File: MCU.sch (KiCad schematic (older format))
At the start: 64 parts, among them J9 Micro_SD_Card_Det_Hirose_DM3AT, SW1 RESET, U11 STM32G474, U12 M95256-WMN6P, U17 ADG706, U5 MCP2562, U6 LTC6259, U8 LTC6820, U9 HM2103

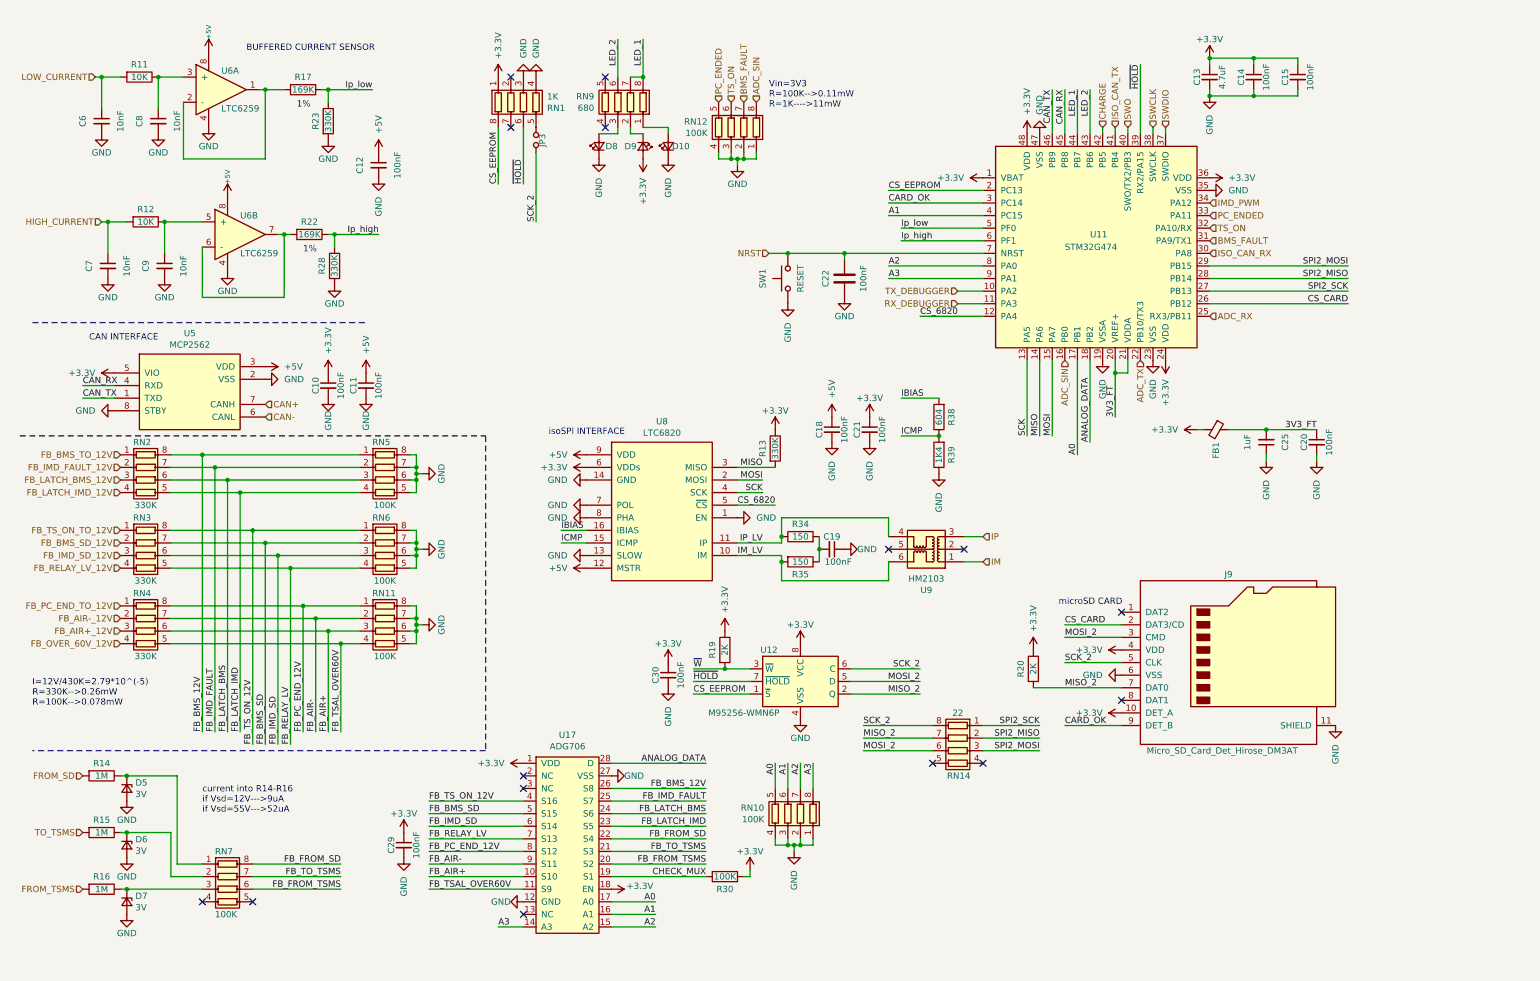
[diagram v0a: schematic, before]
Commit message: added a lot of annotations and readability in the schematic, not complete
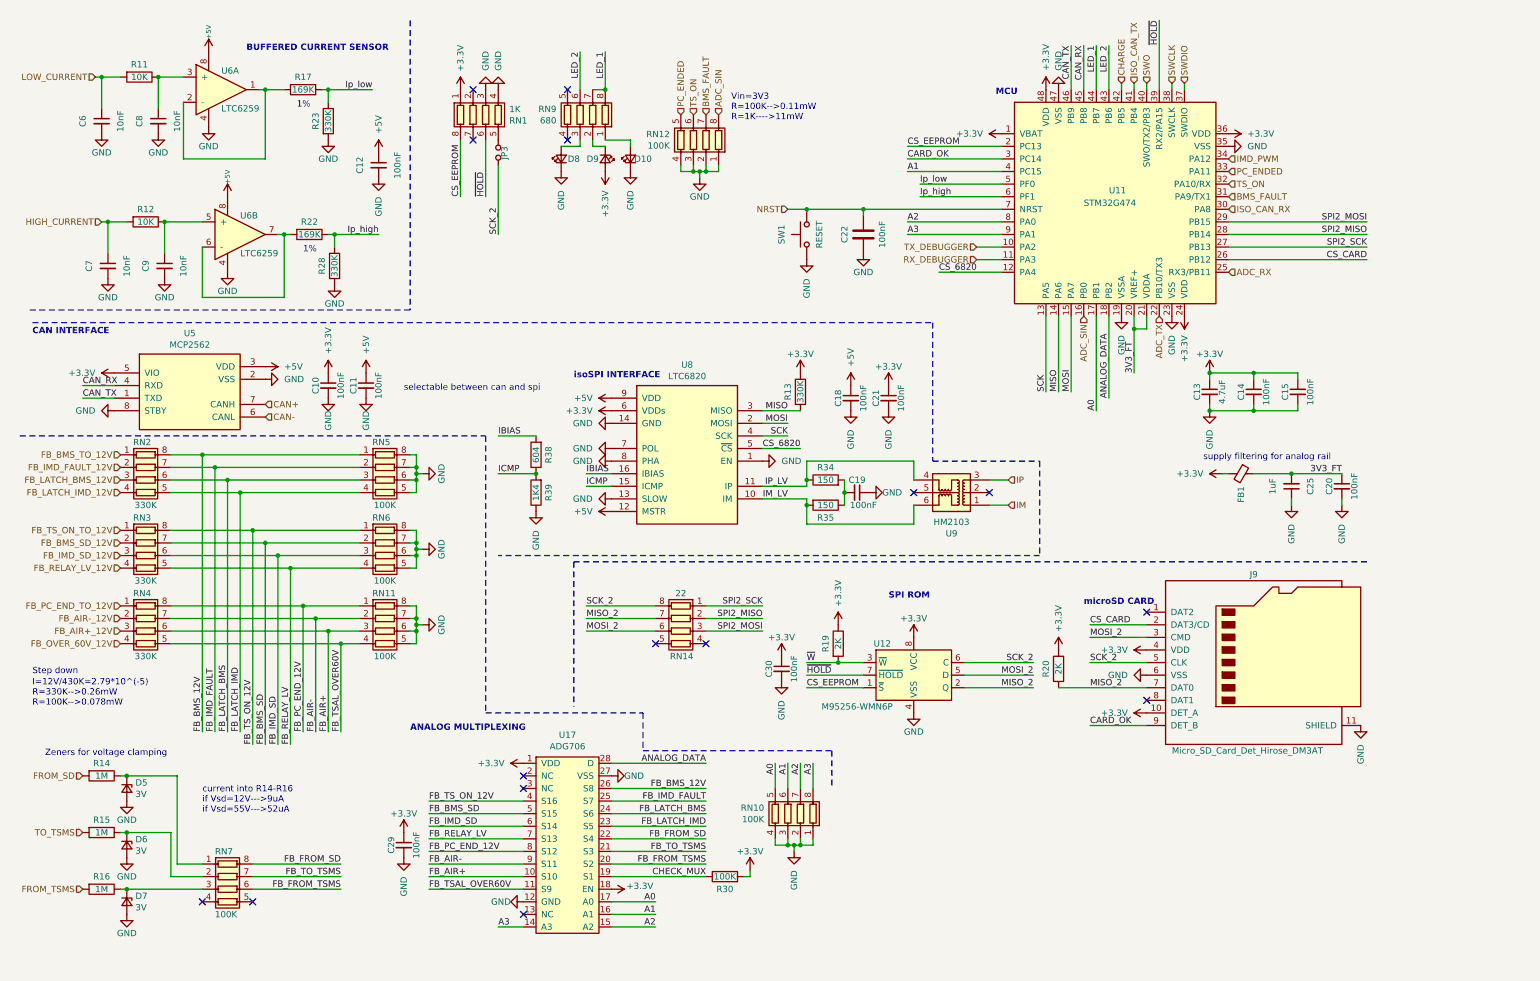
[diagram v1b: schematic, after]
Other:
- note added: "ANALOG MULTIPLEXING"
- note added: "MCU"
- note added: "SPI ROM"
- note added: "Step down"
- note added: "Zeners for voltage clamping"
- note added: "selectable between can and spi"
- note added: "supply filtering for analog rail"
- moved on the sheet: C13, C14, C15, C18, C19, C20, C21, C22, C25, C30, D10, D8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

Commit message: Updated the project to updates in the kicad libraries
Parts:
- FB1: value Ferrite_Bead_Small -> FerriteBead_Small; symbol Device:Ferrite_Bead_Small -> Device:FerriteBead_Small
- JP3: value Jumper_NO_Small -> SolderJumper_2_Open; symbol Device:Jumper_NO_Small -> Jumper:SolderJumper_2_Open
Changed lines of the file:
@@
 $EndComp
 $Comp
-L Device:Ferrite_Bead_Small FB1
+L Device:FerriteBead_Small FB1
 U 1 1 5E60756E
 P 10200 4100
 F 0 "FB1" H 10300 4100 50  0000 L CNN
-F 1 "Ferrite_Bead_Small" H 10300 4055 50  0001 L CNN
+F 1 "FerriteBead_Small" H 10300 4055 50  0001 L CNN
 F 2 "Inductor_SMD:L_0603_1608Metric_Pad1.05x0.95mm_HandSolder" V 10130 4100 50  0001 C CNN
 F 3 "~" H 10200 4100 50  0001 C CNN
@@
 $EndComp
 Wire Wire Line
-	4300 1650 4300 2200
-$Comp
-L Device:Jumper_NO_Small JP3
+	4300 1750 4300 2200
+$Comp
+L Jumper:SolderJumper_2_Open JP3
 U 1 1 5EB0119F
-P 4300 1550
-F 0 "JP3" H 4250 1500 50  0000 L CNN
-F 1 "Jumper_NO_Small" V 4345 1598 50  0001 L CNN
-F 2 "MainBoard:Jumper_SMD_0603" H 4300 1550 50  0001 C CNN
-F 3 "~" H 4300 1550 50  0001 C CNN
-	1    4300 1550
+P 4300 1600
+F 0 "JP3" H 4250 1550 50  0000 L CNN
+F 1 "SolderJumper_2_Open" V 4345 1648 50  0001 L CNN
+F 2 "MainBoard:Jumper_SMD_0603" H 4300 1600 50  0001 C CNN
+F 3 "~" H 4300 1600 50  0001 C CNN
+	1    4300 1600
 	0    -1   1    0
 $EndComp

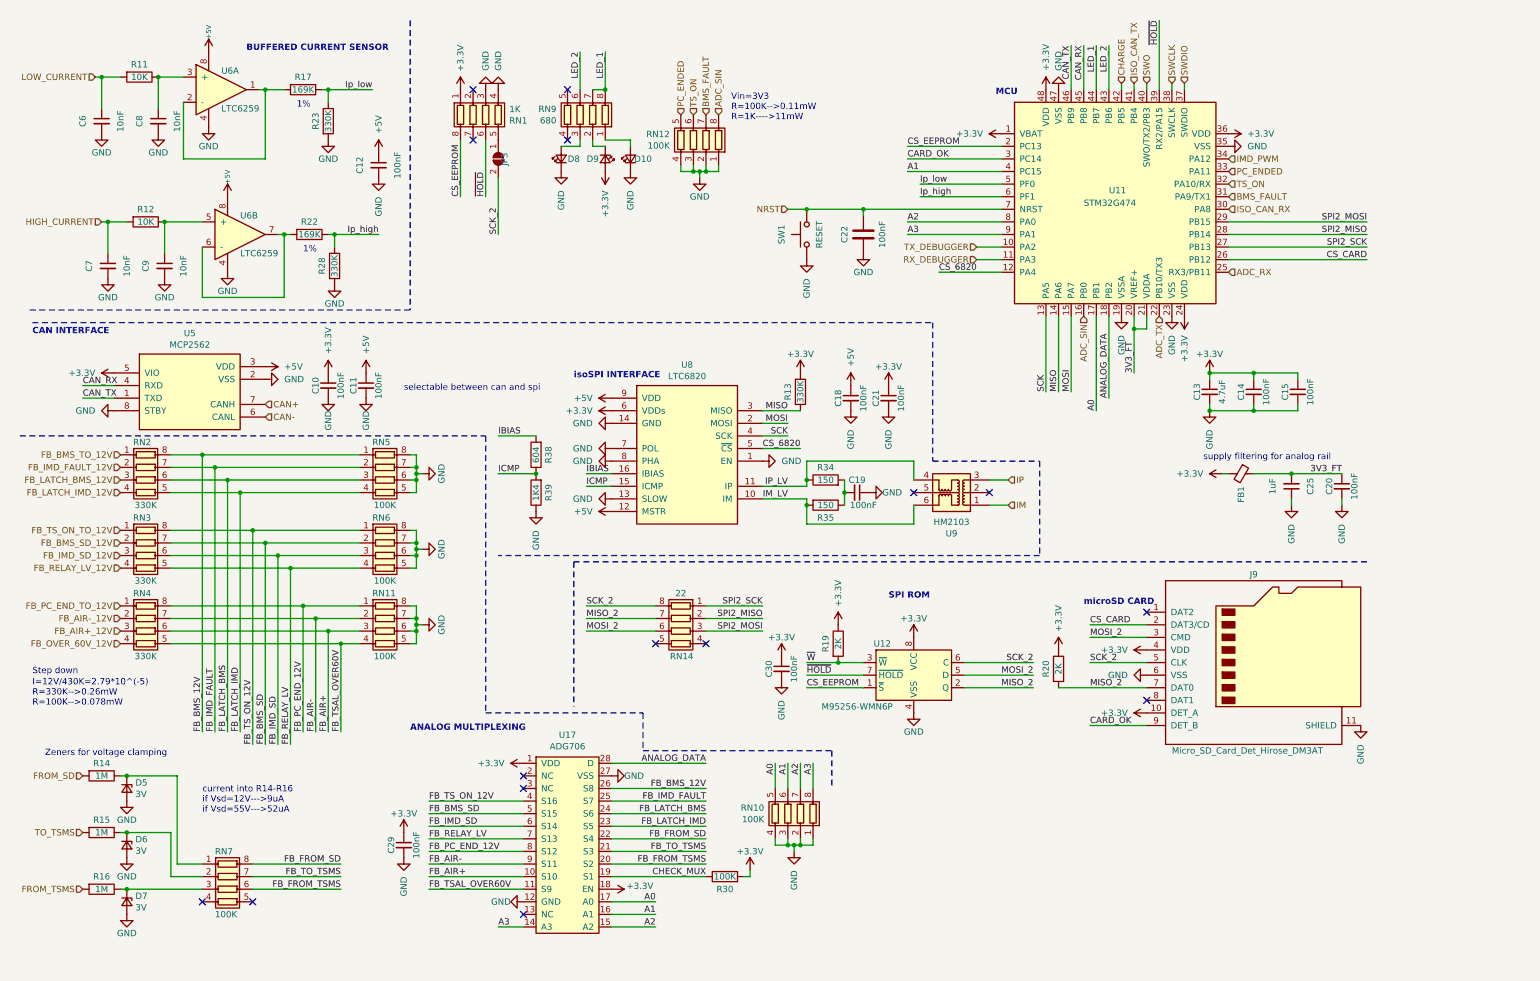
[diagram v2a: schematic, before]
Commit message: updated to new components as per v1.0.5
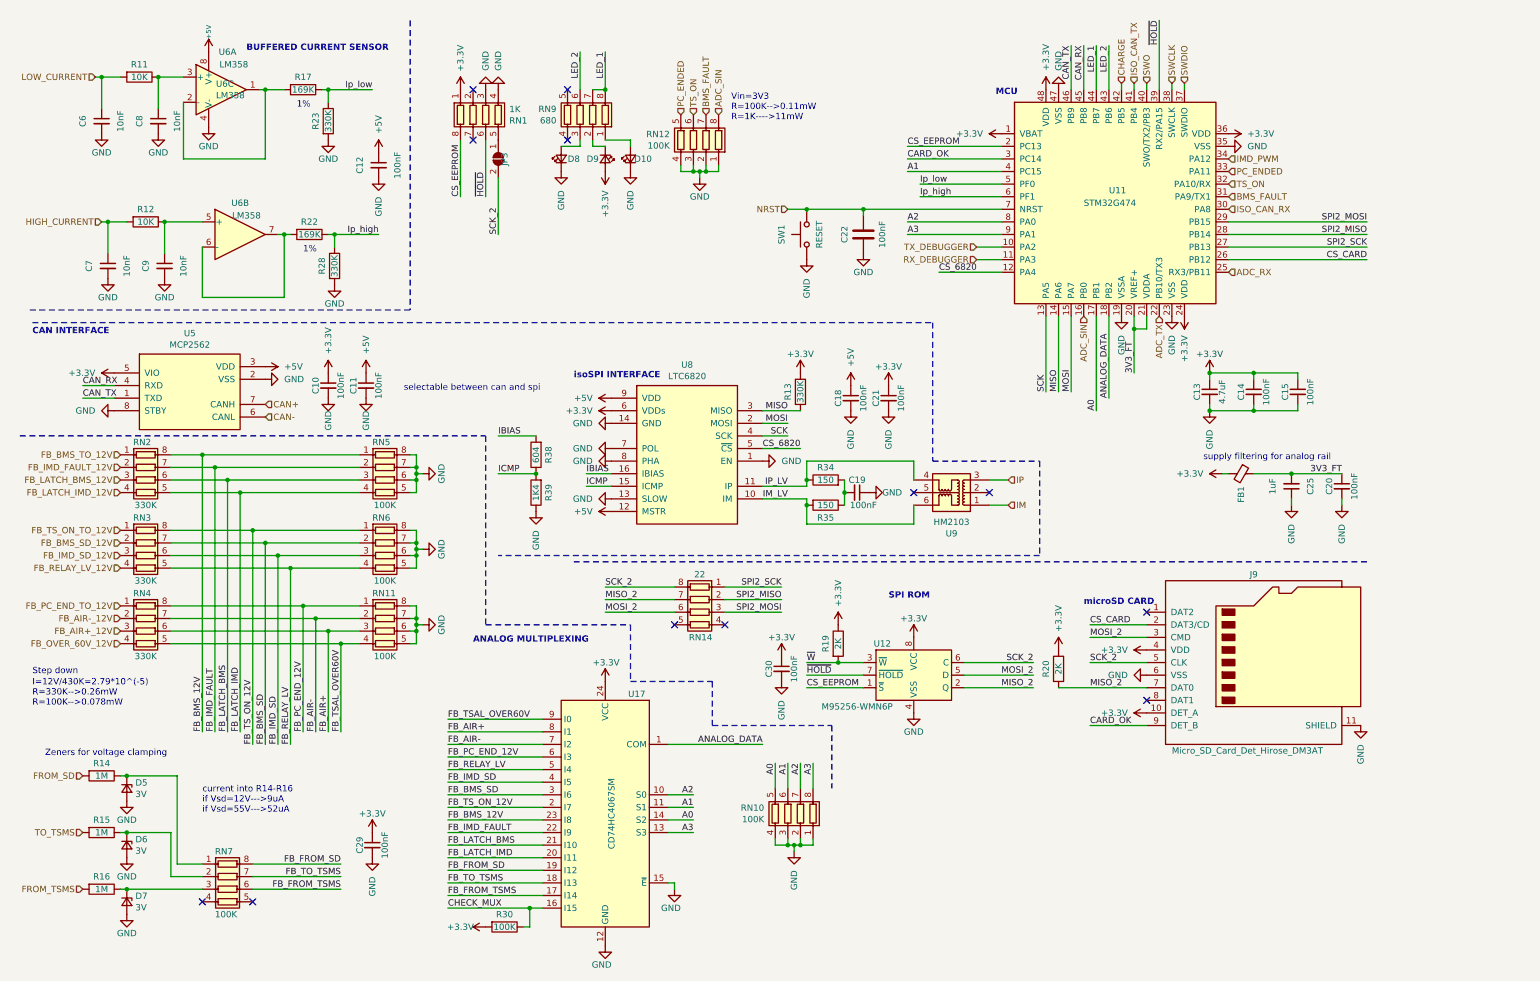
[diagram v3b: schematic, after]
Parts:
- removed U17: ADG706, Package_SO:TSSOP-28_4.4x9.7mm_P0.65mm, symbol MainBoard:ADG706
- removed U6: LTC6259, Package_TO_SOT_SMD:TSOT-23-8, symbol MainBoard:LTC6259
- added U17: CD74HC4067SM, Package_SO:SSOP-24_5.3x8.2mm_P0.65mm, symbol 74xx:CD74HC4067SM
- added U6: LM358, Package_TO_SOT_SMD:TSOT-23-8, symbol Amplifier_Operational:LM358
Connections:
- net +3V3: now also U17.24 (VCC)
- net +5V: now also U6.8 (V+)
- net A0: now also U17.14 (S2)
- net A1: now also U17.11 (S1)
- net A2: now also U17.10 (S0)
- net A3: now also U17.13 (S3)
- net ANALOG_DATA: now also U17.1 (COM)
- net CHECK_MUX: now also U17.16 (I15)
- net FB_AIR+: now also U17.8 (I1)
- net FB_AIR-: now also U17.7 (I2)
- net FB_BMS_12V: now also U17.23 (I8)
- net FB_BMS_SD: now also U17.3 (I6)
- net FB_FROM_SD: now also U17.19 (I12)
- net FB_FROM_TSMS: now also U17.17 (I14)
- net FB_IMD_FAULT: now also U17.22 (I9)
- net FB_IMD_SD: now also U17.4 (I5)
- net FB_LATCH_BMS: now also U17.21 (I10)
- net FB_LATCH_IMD: now also U17.20 (I11)
- net FB_PC_END_12V: now also U17.6 (I3)
- net FB_RELAY_LV: now also U17.5 (I4)
- net FB_TO_TSMS: now also U17.18 (I13)
- net FB_TSAL_OVER60V: now also U17.9 (I0)
- net FB_TS_ON_12V: now also U17.2 (I7)
- net GND: now also U17.12 (GND), U17.15 (~E), U6.4 (V-)
- net at R22.2: now also U6.6 (-), U6.7
- net at C9.1, R12.1: now also U6.5 (+)
- net at C8.1, R11.1: now also U6.3 (+)
- net at R17.2: now also U6.1, U6.2 (-)
- no-connect marks 15 -> 12
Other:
- moved on the sheet: C29, R30, RN14

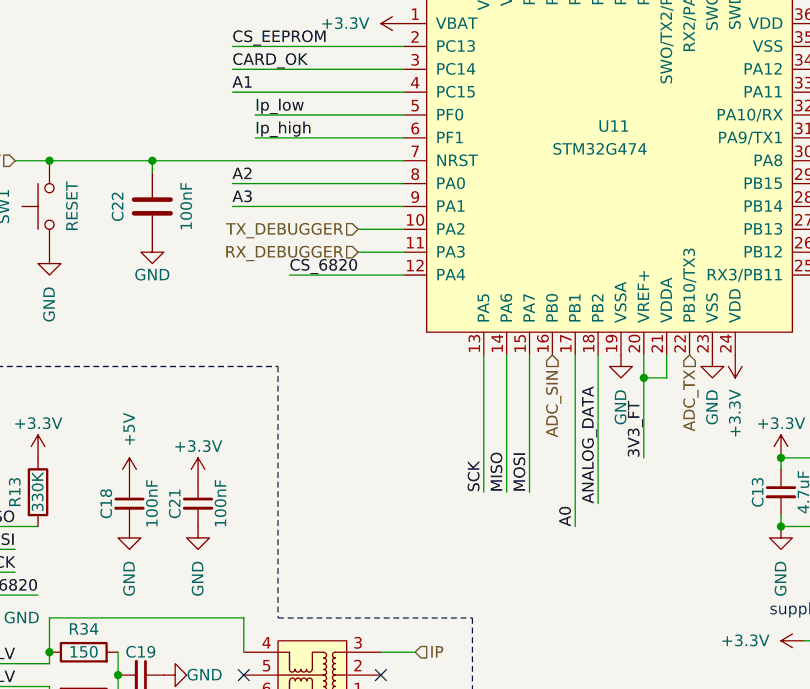
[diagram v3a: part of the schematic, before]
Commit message: Updated all to the last new v1.0.5 as printed by taba
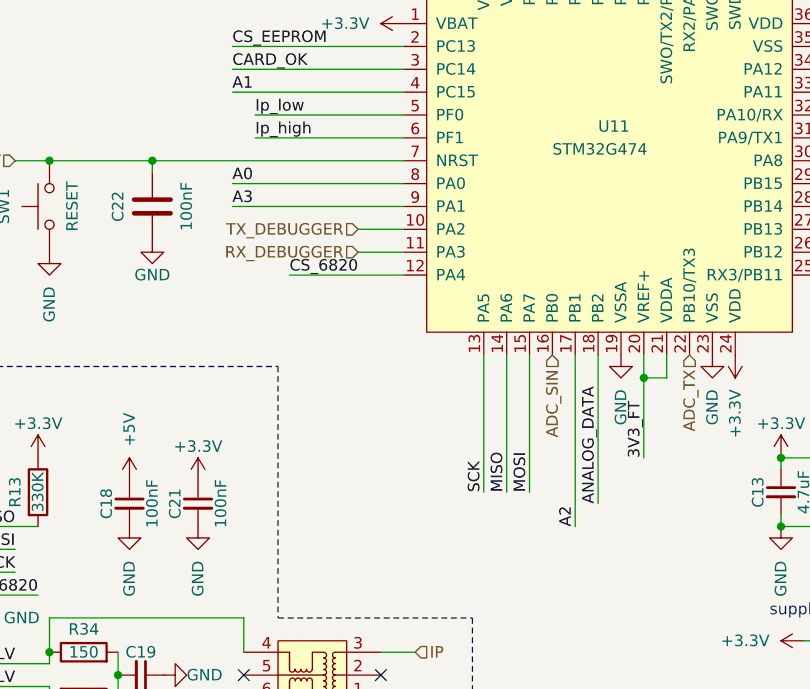
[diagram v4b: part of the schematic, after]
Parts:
- U17: footprint Package_SO:SSOP-24_5.3x8.2mm_P0.65mm -> Package_SO:TSSOP-24_4.4x7.8mm_P0.65mm
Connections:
- net A0: now also U11.8 (PA0); no longer U11.17 (PB1)
- net A2: now also U11.17 (PB1); no longer U11.8 (PA0)
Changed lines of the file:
@@
 Wire Wire Line
 	9050 2850 9050 3600
-Text Label 9050 3600 1    50   ~ 0
+Text Label 7550 2100 0    50   ~ 0
 A0
 Text Label 7550 1700 0    50   ~ 0
 A1
-Text Label 7550 2100 0    50   ~ 0
+Text Label 9050 3600 1    50   ~ 0
 A2
 Wire Wire Line
@@
 F 0 "U17" H 4900 7650 50  0000 C CNN
 F 1 "CD74HC4067SM" V 5100 6700 50  0000 C CNN
-F 2 "Package_SO:SSOP-24_5.3x8.2mm_P0.65mm" H 6200 5750 50  0001 C CIN
+F 2 "Package_SO:TSSOP-24_4.4x7.8mm_P0.65mm" H 6200 5750 50  0001 C CIN
 F 3 "http://www.ti.com/lit/ds/symlink/cd74hc4067.pdf" H 4800 7600 50  0001 C CNN
 	1    5150 6750

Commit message: Board as soldered
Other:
- note added: "Switch this and BOOT0 so to have it work"
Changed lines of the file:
@@
 	1    0    0    -1
 $EndComp
+Text Notes 10550 1750 0    50   ~ 0
+Switch this and BOOT0 so to have it work
 $EndSCHEMATC
